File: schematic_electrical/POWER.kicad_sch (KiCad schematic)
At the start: 4 parts, among them SW1 SW_SPST_Lamp, SW2 SW_SPST_Lamp

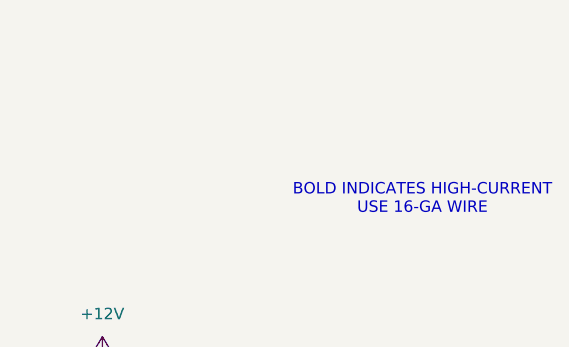
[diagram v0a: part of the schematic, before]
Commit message: Pylon schmatic: clarify filenames and add orange text to avoid confusing other similar schematic pages.
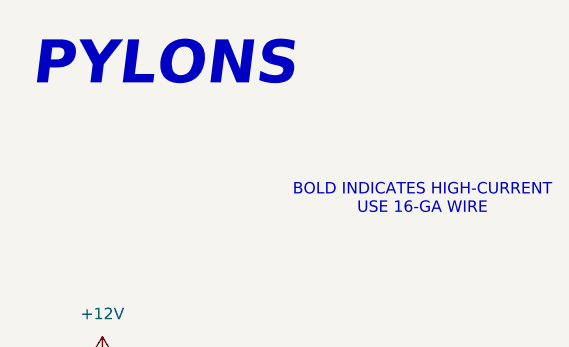
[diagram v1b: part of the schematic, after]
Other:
- note added: "PYLONS"
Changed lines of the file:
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@@
+		)
+	)
+	(text "PYLONS"
+		(exclude_from_sim no)
+		(at 34.798 21.844 0)
+		(effects
+			(font
+				(size 4.7752 4.7752)
+				(thickness 0.955)
+				(bold yes)
+				(italic yes)
+				(color 255 153 0 1)
+			)
 		)
 	)
@@
 		)
 		(instances
-			(project "high_striker_boosh"
+			(project "pylons_boosh_remote_reciver"
 				(path "/f3653ac0-a28a-4ee8-bcf5-236139001455/6657731a-46b5-42dc-8611-bac46a2b6e5c"
 					(reference "SW1")
@@
 		)
 		(instances
-			(project "high_striker_boosh"
+			(project "pylons_boosh_remote_reciver"
 				(path "/f3653ac0-a28a-4ee8-bcf5-236139001455/6657731a-46b5-42dc-8611-bac46a2b6e5c"
 					(reference "F2")
@@
 		)
 		(instances
-			(project "high_striker_boosh"
+			(project "pylons_boosh_remote_reciver"
 				(path "/f3653ac0-a28a-4ee8-bcf5-236139001455/6657731a-46b5-42dc-8611-bac46a2b6e5c"
 					(reference "#PWR038")
@@
 		)
 		(instances
-			(project "high_striker_boosh"
+			(project "pylons_boosh_remote_reciver"
 				(path "/f3653ac0-a28a-4ee8-bcf5-236139001455/6657731a-46b5-42dc-8611-bac46a2b6e5c"
 					(reference "#PWR044")
@@
 		)
 		(instances
-			(project "high_striker_boosh"
+			(project "pylons_boosh_remote_reciver"
 				(path "/f3653ac0-a28a-4ee8-bcf5-236139001455/6657731a-46b5-42dc-8611-bac46a2b6e5c"
 					(reference "F1")
@@
 		)
 		(instances
-			(project "high_striker_boosh"
+			(project "pylons_boosh_remote_reciver"
 				(path "/f3653ac0-a28a-4ee8-bcf5-236139001455/6657731a-46b5-42dc-8611-bac46a2b6e5c"
 					(reference "#PWR036")
@@
 		)
 		(instances
-			(project "high_striker_boosh"
+			(project "pylons_boosh_remote_reciver"
 				(path "/f3653ac0-a28a-4ee8-bcf5-236139001455/6657731a-46b5-42dc-8611-bac46a2b6e5c"
 					(reference "#PWR045")
@@
 		)
 		(instances
-			(project "high_striker_boosh"
+			(project "pylons_boosh_remote_reciver"
 				(path "/f3653ac0-a28a-4ee8-bcf5-236139001455/6657731a-46b5-42dc-8611-bac46a2b6e5c"
 					(reference "#PWR037")
@@
 		)
 		(instances
-			(project "high_striker_boosh"
+			(project "pylons_boosh_remote_reciver"
 				(path "/f3653ac0-a28a-4ee8-bcf5-236139001455/6657731a-46b5-42dc-8611-bac46a2b6e5c"
 					(reference "#PWR043")
@@
 		)
 		(instances
-			(project "high_striker_boosh"
+			(project "pylons_boosh_remote_reciver"
 				(path "/f3653ac0-a28a-4ee8-bcf5-236139001455/6657731a-46b5-42dc-8611-bac46a2b6e5c"
 					(reference "SW2")
@@
 		)
 		(instances
-			(project "high_striker_boosh"
+			(project "pylons_boosh_remote_reciver"
 				(path "/f3653ac0-a28a-4ee8-bcf5-236139001455/6657731a-46b5-42dc-8611-bac46a2b6e5c"
 					(reference "#PWR046")

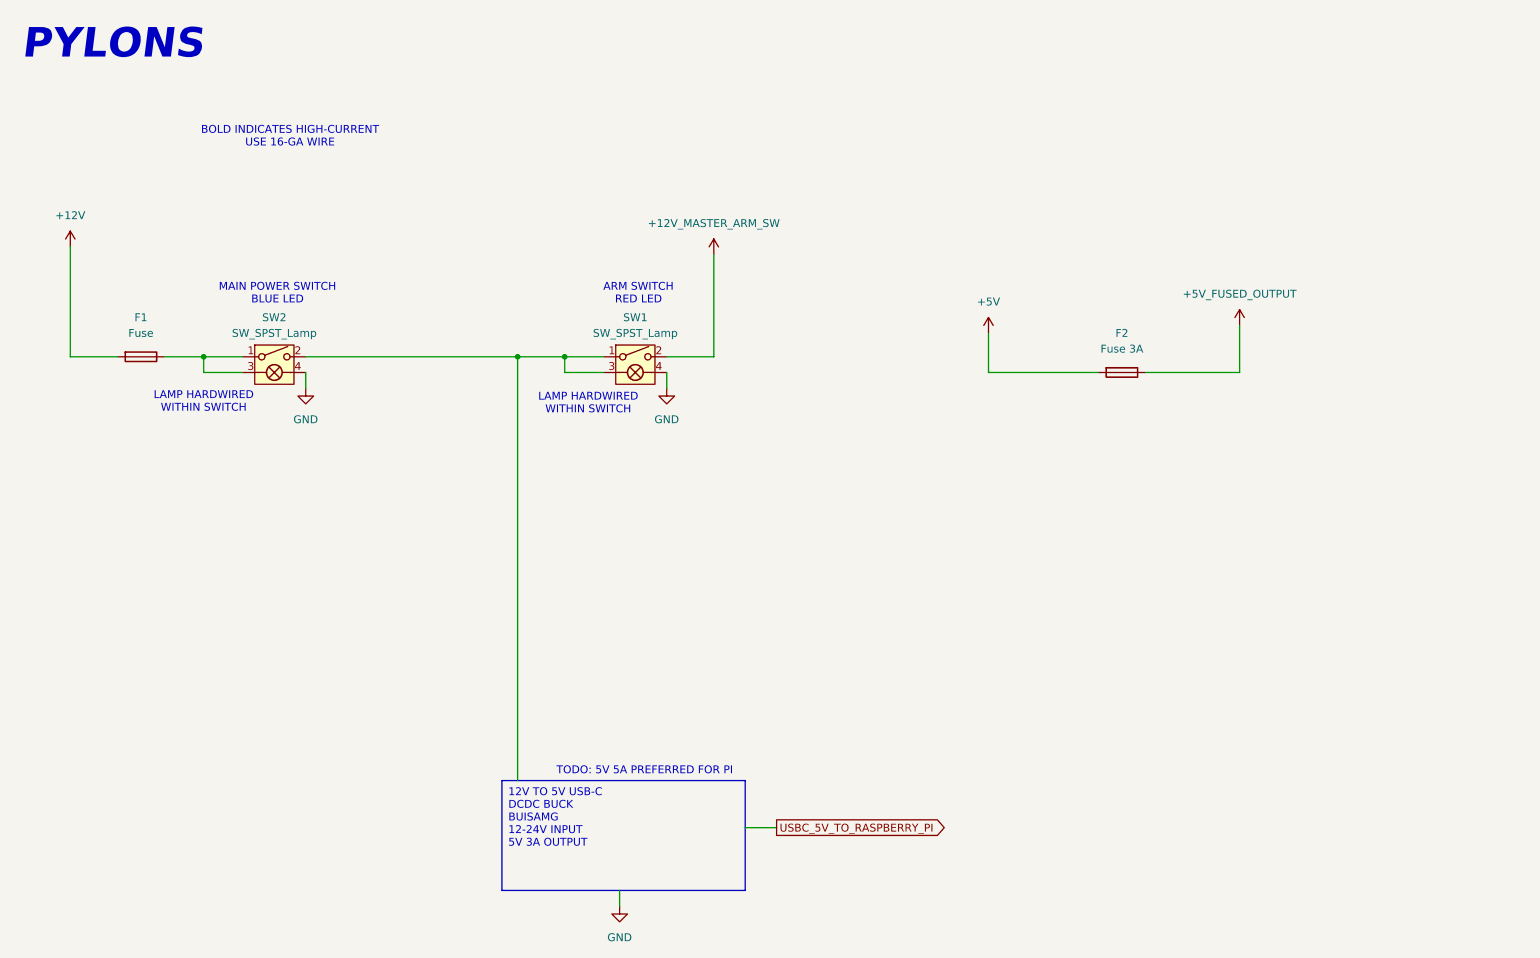
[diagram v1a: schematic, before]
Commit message: Schematic for fabrication. New symbols
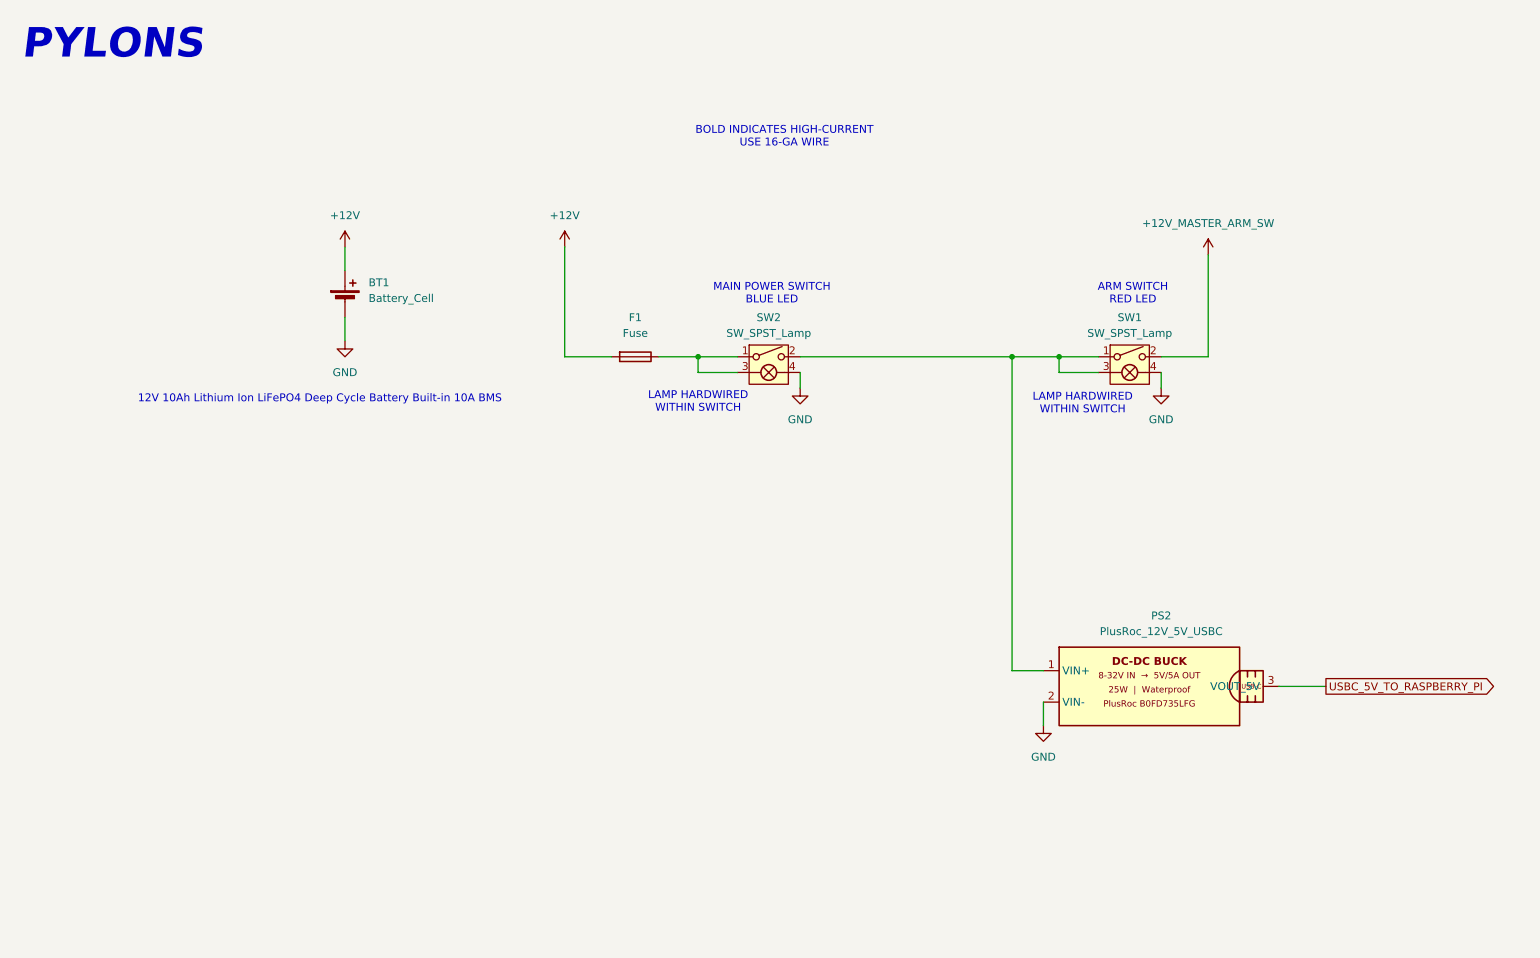
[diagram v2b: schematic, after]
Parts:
- removed F2: Fuse 3A, symbol Device:Fuse
- added BT1: Battery_Cell, symbol Device:Battery_Cell
- added PS2: PlusRoc_12V_5V_USBC, symbol plusroc_12v_5v_usbc:PlusRoc_12V_5V_USBC
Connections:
- net +12V: now also BT1.1 (+)
- net GND: now also BT1.2 (-), PS2.2 (VIN-)
- net USBC_5V_TO_RASPBERRY_PI: now also PS2.3 (VOUT_5V)
- net at SW1.1, SW1.3 (L), SW2.2: now also PS2.1 (VIN+)
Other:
- note added: "12V 10Ah Lithium Ion LiFePO4 Deep Cycle Battery Built-in 10A BMS"
- note removed: "TODO: 5V 5A PREFERRED FOR PI"
- moved on the sheet: F1, SW1, SW2

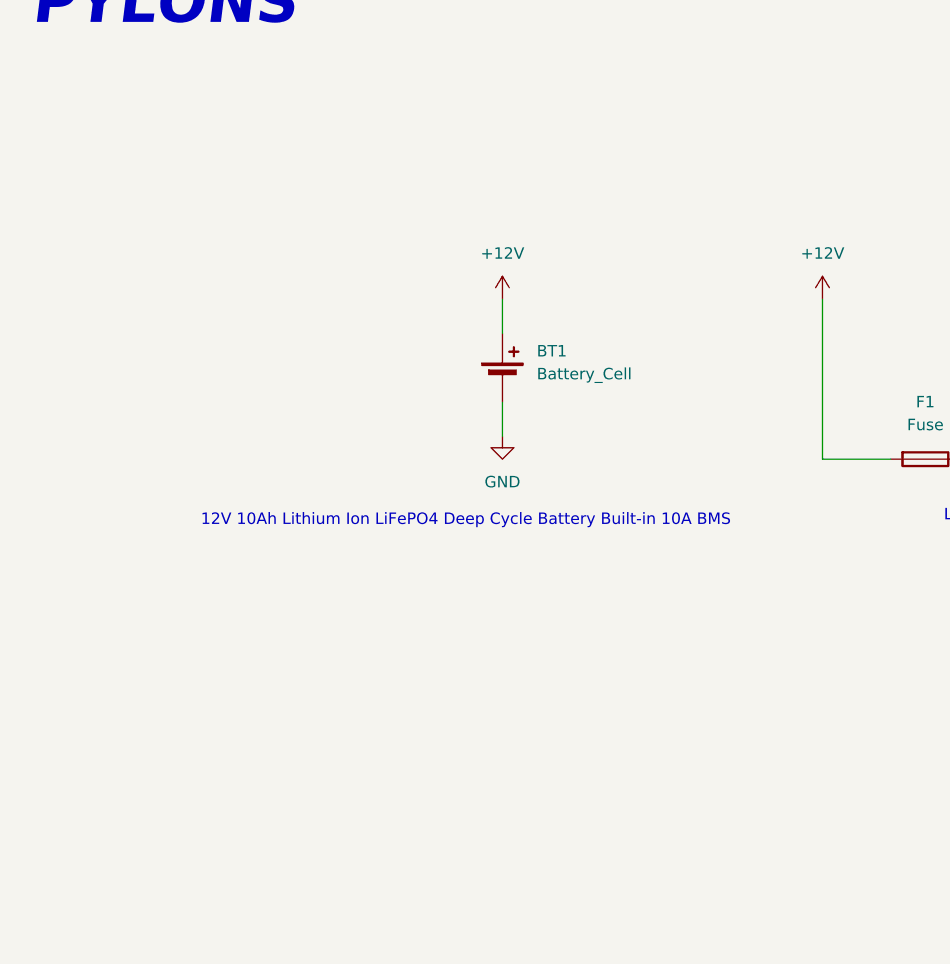
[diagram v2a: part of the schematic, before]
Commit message: scehmatic power options cleanup and LED actual as built
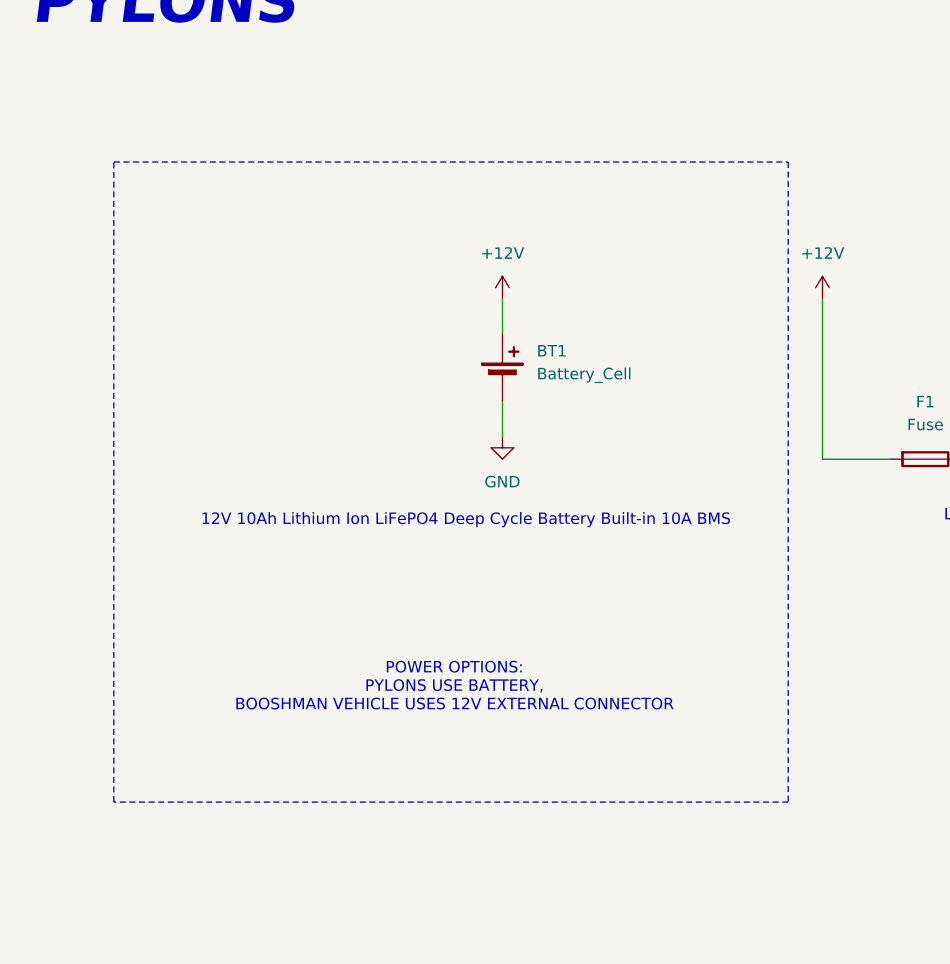
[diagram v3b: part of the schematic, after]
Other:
- note added: "POWER OPTIONS: PYLONS USE BATTERY, BOOSHMAN VEHICLE USES 12V EXTERNAL CONNECTOR"
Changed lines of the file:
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@@
+		)
+	)
+	(rectangle
+		(start 29.21 39.37)
+		(end 104.14 110.49)
+		(stroke
+			(width 0)
+			(type dash)
+		)
+		(fill
+			(type none)
 		)
 	)
@@
 		(effects
 			(font
+				(size 1.27 1.27)
+			)
+		)
+	)
+	(text "POWER OPTIONS:\nPYLONS USE BATTERY,\nBOOSHMAN VEHICLE USES 12V EXTERNAL CONNECTOR"
+		(exclude_from_sim no)
+		(at 67.056 97.79 0)
+		(effects
+			(font

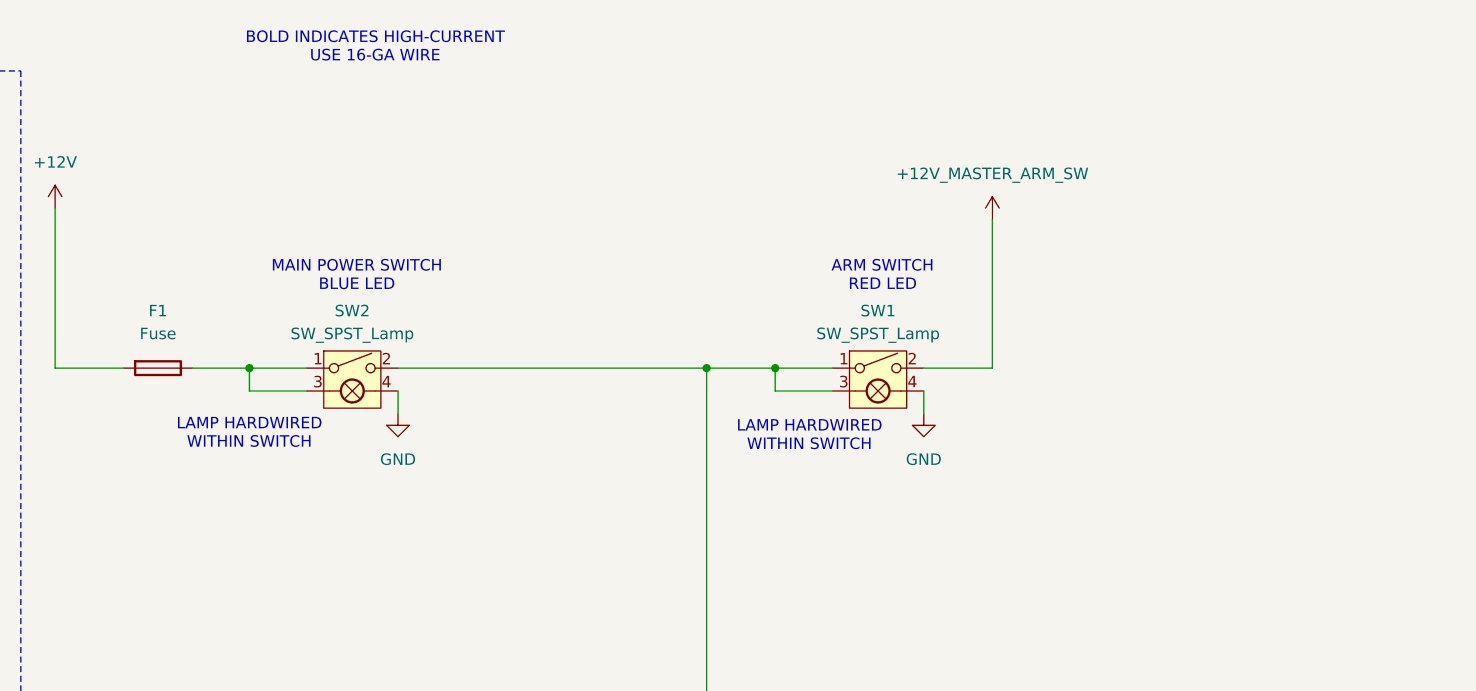
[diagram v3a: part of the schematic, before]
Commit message: Schematic symbols and cleanup for building board
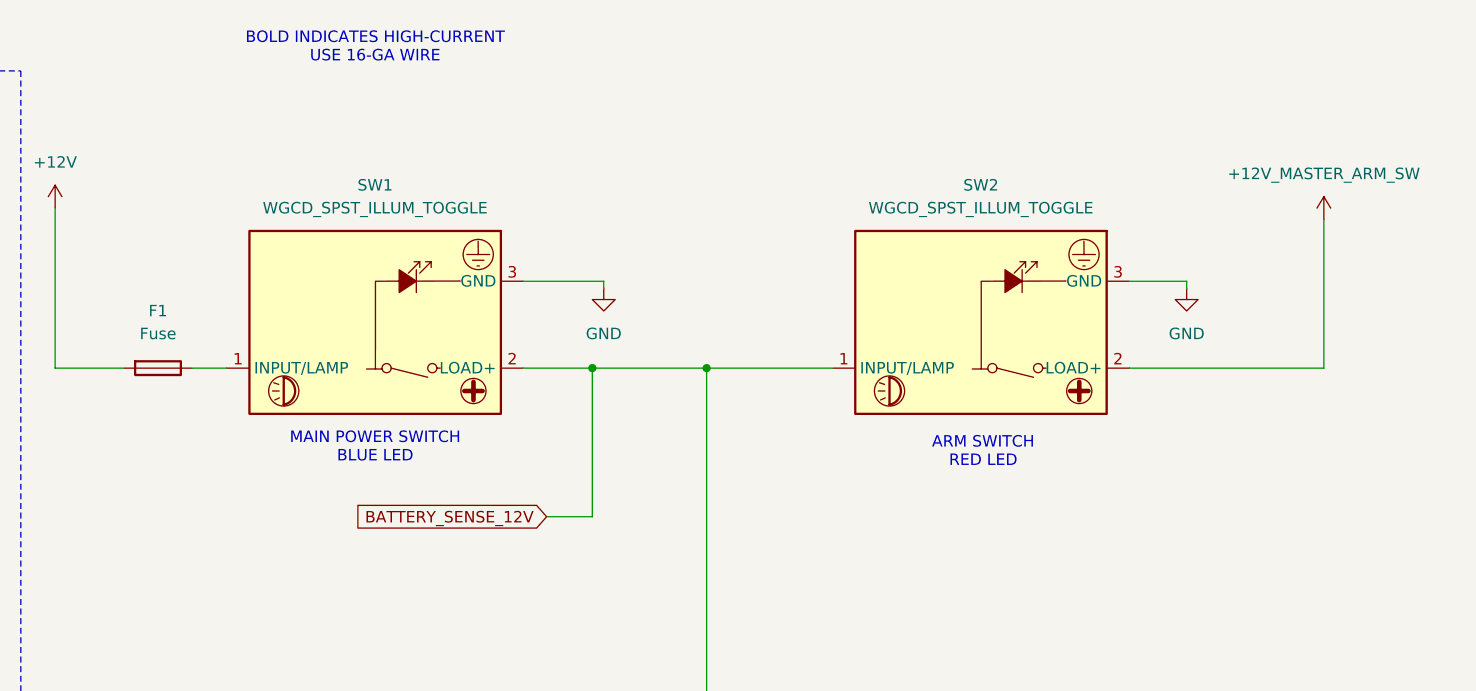
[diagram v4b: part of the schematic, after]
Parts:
- removed SW1, SW2: SW_SPST_Lamp, symbol Switch:SW_SPST_Lamp
- added SW1, SW2: WGCD_SPST_ILLUM_TOGGLE, symbol wgcd_spst_illum_toggle:WGCD_SPST_ILLUM_TOGGLE
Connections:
- net +12V_MASTER_ARM_SW: now also SW2.2 (LOAD+)
- net GND: now also SW1.3 (GND), SW2.3 (GND)
- net BATTERY_SENSE_12V: now reaches PS2.1 (VIN+)
- net BATTERY_SENSE_12V: now also SW1.2 (LOAD+), SW2.1 (INPUT/LAMP)
- net at F1.1: now also SW1.1 (INPUT/LAMP)
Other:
- note removed: "LAMP HARDWIRED WITHIN SWITCH"
